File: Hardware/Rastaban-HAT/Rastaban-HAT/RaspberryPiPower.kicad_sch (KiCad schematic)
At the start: 19 parts, among them IC2 DMMT5401-7-F, Q3 DMG2305UX-7, U5 RT7272AGSP

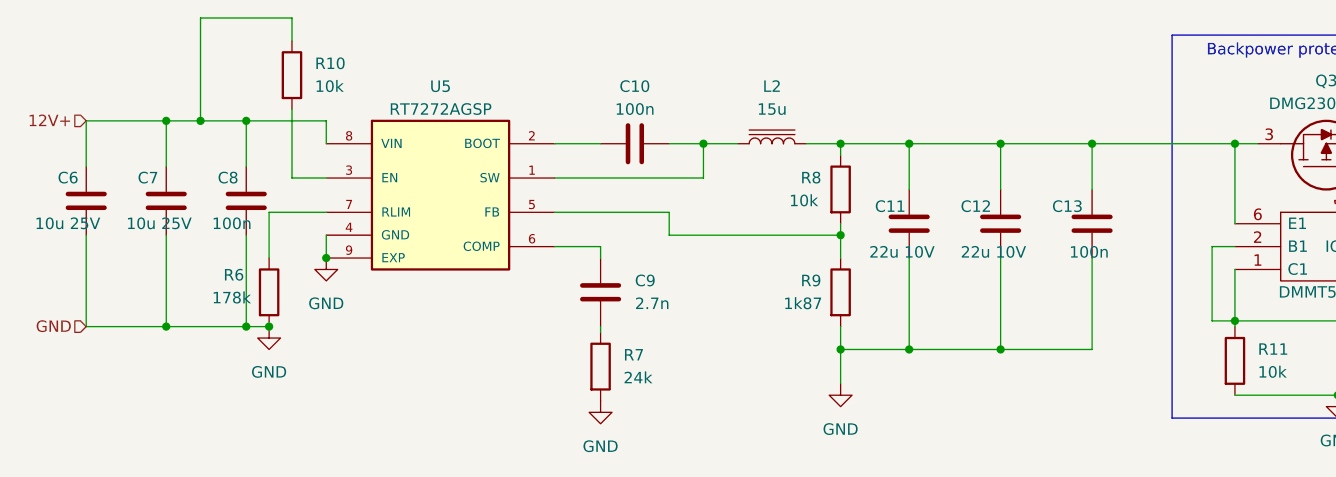
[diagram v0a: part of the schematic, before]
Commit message: added new libarries and jlcpcb part plugin
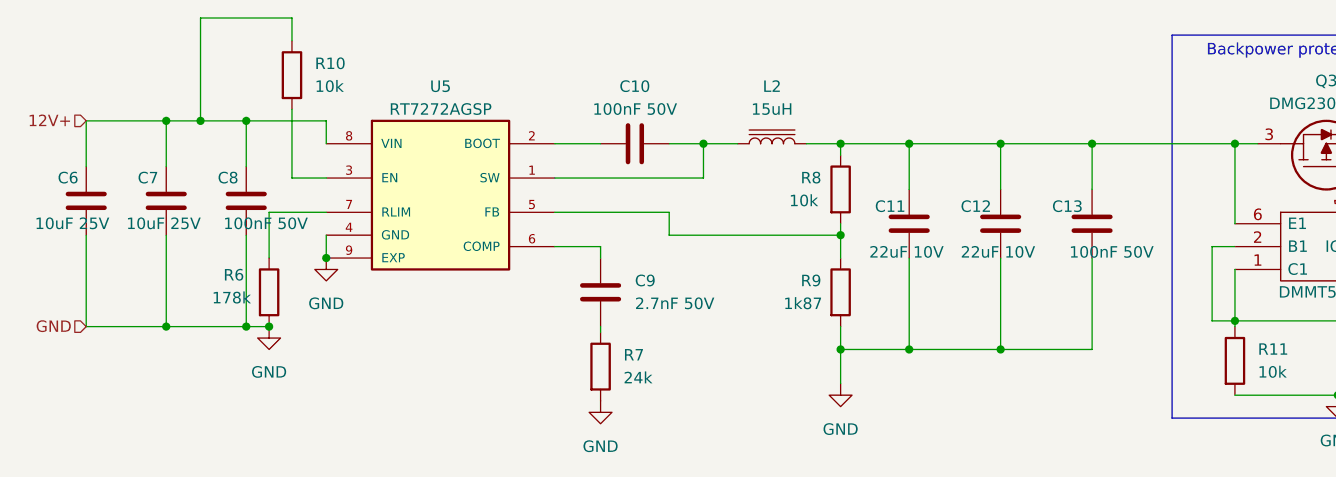
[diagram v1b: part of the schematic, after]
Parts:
- C10, C13, C8: value 100n -> 100nF 50V; footprint Capacitor_SMD:C_1206_3216Metric_Pad1.33x1.80mm_HandSolder -> Capacitor_SMD:C_0805_2012Metric_Pad1.18x1.45mm_HandSolder
- C11, C12: value 22u 10V -> 22uF 10V; footprint Capacitor_SMD:C_1206_3216Metric_Pad1.33x1.80mm_HandSolder -> Capacitor_SMD:C_0805_2012Metric_Pad1.18x1.45mm_HandSolder
- C6, C7: value 10u 25V -> 10uF 25V; footprint Capacitor_SMD:C_1206_3216Metric_Pad1.33x1.80mm_HandSolder -> Capacitor_SMD:C_0805_2012Metric_Pad1.18x1.45mm_HandSolder
- C9: value 2.7n -> 2.7nF 50V; footprint Capacitor_SMD:C_1206_3216Metric_Pad1.33x1.80mm_HandSolder -> Capacitor_SMD:C_0805_2012Metric_Pad1.18x1.45mm_HandSolder
- IC2: footprint SmacSYs:SOT95P285X140-6N -> SamacSys_Parts:SOT95P285X140-6N
- L2: value 15u -> 15uH
- Q3: footprint Snapeda:SOT91P240X110-3N_DMG2305UX-7 -> Package_TO_SOT_SMD:SOT-23
- R10, R11, R12, R6, R7, R8, R9: footprint Resistor_SMD:R_1206_3216Metric_Pad1.30x1.75mm_HandSolder -> Resistor_SMD:R_0805_2012Metric_Pad1.20x1.40mm_HandSolder
- U5: footprint Snapeda:SOIC127P599X175-9N -> (none)
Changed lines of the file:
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@@
       (effects (font (size 1.27 1.27)) (justify left))
     )
-    (property "Footprint" "Resistor_SMD:R_1206_3216Metric_Pad1.30x1.75mm_HandSolder" (id 2) (at 243.967 118.11 90)
+    (property "Footprint" "Resistor_SMD:R_0805_2012Metric_Pad1.20x1.40mm_HandSolder" (id 2) (at 243.967 118.11 90)
       (effects (font (size 1.27 1.27)) hide)
     )
@@
     (property "Reference" "Q3" (id 0) (at 233.045 86.995 90))
     (property "Value" "DMG2305UX-7" (id 1) (at 233.045 89.535 90))
-    (property "Footprint" "Snapeda:SOT91P240X110-3N_DMG2305UX-7" (id 2) (at 236.855 90.17 0)
+    (property "Footprint" "Package_TO_SOT_SMD:SOT-23" (id 2) (at 236.855 90.17 0)
       (effects (font (size 1.27 1.27)) (justify left) hide)
     )
@@
       (effects (font (size 1.27 1.27)) (justify left))
     )
-    (property "Footprint" "Resistor_SMD:R_1206_3216Metric_Pad1.30x1.75mm_HandSolder" (id 2) (at 116.332 86.36 90)
+    (property "Footprint" "Resistor_SMD:R_0805_2012Metric_Pad1.20x1.40mm_HandSolder" (id 2) (at 116.332 86.36 90)
       (effects (font (size 1.27 1.27)) hide)
     )
@@
       (effects (font (size 1.27 1.27)) (justify left))
     )
-    (property "Footprint" "Resistor_SMD:R_1206_3216Metric_Pad1.30x1.75mm_HandSolder" (id 2) (at 150.622 118.745 90)
+    (property "Footprint" "Resistor_SMD:R_0805_2012Metric_Pad1.20x1.40mm_HandSolder" (id 2) (at 150.622 118.745 90)
       (effects (font (size 1.27 1.27)) hide)
     )
@@
       (effects (font (size 1.27 1.27)) (justify left))
     )
-    (property "Footprint" "Resistor_SMD:R_1206_3216Metric_Pad1.30x1.75mm_HandSolder" (id 2) (at 113.792 110.49 90)
+    (property "Footprint" "Resistor_SMD:R_0805_2012Metric_Pad1.20x1.40mm_HandSolder" (id 2) (at 113.792 110.49 90)
       (effects (font (size 1.27 1.27)) hide)
     )
@@
       (effects (font (size 1.27 1.27)) (justify left))
     )
-    (property "Footprint" "Resistor_SMD:R_1206_3216Metric_Pad1.30x1.75mm_HandSolder" (id 2) (at 221.107 118.11 90)
+    (property "Footprint" "Resistor_SMD:R_0805_2012Metric_Pad1.20x1.40mm_HandSolder" (id 2) (at 221.107 118.11 90)
       (effects (font (size 1.27 1.27)) hide)
     )
@@
       (effects (font (size 1.27 1.27)) (justify right))
     )
-    (property "Value" "22u 10V" (id 1) (at 182.245 106.045 0)
-      (effects (font (size 1.27 1.27)) (justify right))
-    )
-    (property "Footprint" "Capacitor_SMD:C_1206_3216Metric_Pad1.33x1.80mm_HandSolder" (id 2) (at 185.7248 99.06 0)
+    (property "Value" "22uF 10V" (id 1) (at 182.245 106.045 0)
+      (effects (font (size 1.27 1.27)) (justify right))
+    )
+    (property "Footprint" "Capacitor_SMD:C_0805_2012Metric_Pad1.18x1.45mm_HandSolder" (id 2) (at 185.7248 99.06 0)
       (effects (font (size 1.27 1.27)) hide)
     )
@@
       (effects (font (size 1.27 1.27)) (justify left))
     )
-    (property "Value" "10u 25V" (id 1) (at 89.535 102.87 0)
-      (effects (font (size 1.27 1.27)) (justify left))
-    )
-    (property "Footprint" "Capacitor_SMD:C_1206_3216Metric_Pad1.33x1.80mm_HandSolder" (id 2) (at 96.2152 104.14 0)
+    (property "Value" "10uF 25V" (id 1) (at 89.535 102.87 0)
+      (effects (font (size 1.27 1.27)) (justify left))
+    )
+    (property "Footprint" "Capacitor_SMD:C_0805_2012Metric_Pad1.18x1.45mm_HandSolder" (id 2) (at 96.2152 104.14 0)
       (effects (font (size 1.27 1.27)) hide)
     )
@@
       (effects (font (size 1.27 1.27)) (justify right))
     )
-    (property "Value" "100n" (id 1) (at 204.47 106.045 0)
-      (effects (font (size 1.27 1.27)) (justify right))
-    )
-    (property "Footprint" "Capacitor_SMD:C_1206_3216Metric_Pad1.33x1.80mm_HandSolder" (id 2) (at 206.0448 99.06 0)
+    (property "Value" "100nF 50V" (id 1) (at 204.47 106.045 0)
+      (effects (font (size 1.27 1.27)) (justify right))
+    )
+    (property "Footprint" "Capacitor_SMD:C_0805_2012Metric_Pad1.18x1.45mm_HandSolder" (id 2) (at 206.0448 99.06 0)
       (effects (font (size 1.27 1.27)) hide)
     )
@@
       (effects (font (size 1.27 1.27)) (justify left))
     )
-    (property "Value" "10u 25V" (id 1) (at 99.695 102.87 0)
-      (effects (font (size 1.27 1.27)) (justify left))
-    )
-    (property "Footprint" "Capacitor_SMD:C_1206_3216Metric_Pad1.33x1.80mm_HandSolder" (id 2) (at 105.1052 104.14 0)
+    (property "Value" "10uF 25V" (id 1) (at 99.695 102.87 0)
+      (effects (font (size 1.27 1.27)) (justify left))
+    )
+    (property "Footprint" "Capacitor_SMD:C_0805_2012Metric_Pad1.18x1.45mm_HandSolder" (id 2) (at 105.1052 104.14 0)
       (effects (font (size 1.27 1.27)) hide)
     )
@@
     (property "Reference" "U5" (id 0) (at 134.62 87.63 0))
     (property "Value" "RT7272AGSP" (id 1) (at 134.62 90.17 0))
-    (property "Footprint" "Snapeda:SOIC127P599X175-9N" (id 2) (at 127 110.49 0)
+    (property "Footprint" "" (id 2) (at 127 110.49 0)
       (effects (font (size 1.27 1.27)) (justify left bottom) hide)
     )
@@
       (effects (font (size 1.27 1.27)) (justify right))
     )
-    (property "Value" "2.7n" (id 1) (at 156.21 111.7599 0)
-      (effects (font (size 1.27 1.27)) (justify right))
-    )
-    (property "Footprint" "Capacitor_SMD:C_1206_3216Metric_Pad1.33x1.80mm_HandSolder" (id 2) (at 151.4348 106.68 0)
+    (property "Value" "2.7nF 50V" (id 1) (at 156.21 111.7599 0)
+      (effects (font (size 1.27 1.27)) (justify right))
+    )
+    (property "Footprint" "Capacitor_SMD:C_0805_2012Metric_Pad1.18x1.45mm_HandSolder" (id 2) (at 151.4348 106.68 0)
       (effects (font (size 1.27 1.27)) hide)
     )
@@
     (property "Reference" "IC2" (id 0) (at 234.315 105.41 0))
     (property "Value" "DMMT5401-7-F" (id 1) (at 234.315 110.49 0))
-    (property "Footprint" "SmacSYs:SOT95P285X140-6N" (id 2) (at 241.935 100.33 0)
+    (property "Footprint" "SamacSys_Parts:SOT95P285X140-6N" (id 2) (at 241.935 100.33 0)
       (effects (font (size 1.27 1.27)) (justify left) hide)
     )
@@
       (effects (font (size 1.27 1.27)) (justify right))
     )
-    (property "Value" "22u 10V" (id 1) (at 192.405 106.045 0)
-      (effects (font (size 1.27 1.27)) (justify right))
-    )
-    (property "Footprint" "Capacitor_SMD:C_1206_3216Metric_Pad1.33x1.80mm_HandSolder" (id 2) (at 195.8848 99.06 0)
+    (property "Value" "22uF 10V" (id 1) (at 192.405 106.045 0)
+      (effects (font (size 1.27 1.27)) (justify right))
+    )
+    (property "Footprint" "Capacitor_SMD:C_0805_2012Metric_Pad1.18x1.45mm_HandSolder" (id 2) (at 195.8848 99.06 0)
       (effects (font (size 1.27 1.27)) hide)
     )
@@
       (effects (font (size 1.27 1.27)) (justify left))
     )
-    (property "Footprint" "Resistor_SMD:R_1206_3216Metric_Pad1.30x1.75mm_HandSolder" (id 2) (at 177.292 99.06 90)
+    (property "Footprint" "Resistor_SMD:R_0805_2012Metric_Pad1.20x1.40mm_HandSolder" (id 2) (at 177.292 99.06 90)
       (effects (font (size 1.27 1.27)) hide)
     )
@@
       (effects (font (size 1.27 1.27)) (justify left))
     )
-    (property "Footprint" "Resistor_SMD:R_1206_3216Metric_Pad1.30x1.75mm_HandSolder" (id 2) (at 177.292 110.49 90)
+    (property "Footprint" "Resistor_SMD:R_0805_2012Metric_Pad1.20x1.40mm_HandSolder" (id 2) (at 177.292 110.49 90)
       (effects (font (size 1.27 1.27)) hide)
     )
@@
     (in_bom yes) (on_board yes)
     (property "Reference" "C10" (id 0) (at 156.21 87.63 90))
-    (property "Value" "100n" (id 1) (at 156.21 90.17 90))
-    (property "Footprint" "Capacitor_SMD:C_1206_3216Metric_Pad1.33x1.80mm_HandSolder" (id 2) (at 160.02 93.0148 0)
+    (property "Value" "100nF 50V" (id 1) (at 156.21 90.17 90))
+    (property "Footprint" "Capacitor_SMD:C_0805_2012Metric_Pad1.18x1.45mm_HandSolder" (id 2) (at 160.02 93.0148 0)
       (effects (font (size 1.27 1.27)) hide)
     )
@@
       (effects (font (size 1.27 1.27)) (justify left))
     )
-    (property "Value" "100n" (id 1) (at 109.22 102.87 0)
-      (effects (font (size 1.27 1.27)) (justify left))
-    )
-    (property "Footprint" "Capacitor_SMD:C_1206_3216Metric_Pad1.33x1.80mm_HandSolder" (id 2) (at 113.9952 104.14 0)
+    (property "Value" "100nF 50V" (id 1) (at 110.49 102.87 0)
+      (effects (font (size 1.27 1.27)) (justify left))
+    )
+    (property "Footprint" "Capacitor_SMD:C_0805_2012Metric_Pad1.18x1.45mm_HandSolder" (id 2) (at 113.9952 104.14 0)
       (effects (font (size 1.27 1.27)) hide)
     )
@@
     (in_bom yes) (on_board yes) (fields_autoplaced)
     (property "Reference" "L2" (id 0) (at 171.45 87.63 90))
-    (property "Value" "15u" (id 1) (at 171.45 90.17 90))
+    (property "Value" "15uH" (id 1) (at 171.45 90.17 90))
     (property "Footprint" "Inductor_SMD:L_1206_3216Metric_Pad1.22x1.90mm_HandSolder" (id 2) (at 171.45 93.98 0)
       (effects (font (size 1.27 1.27)) hide)

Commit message: updated footprints
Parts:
- U5: footprint (none) -> SnapEDA Library:SOIC127P599X175-9N
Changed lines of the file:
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@@
     (property "Reference" "U5" (id 0) (at 134.62 87.63 0))
     (property "Value" "RT7272AGSP" (id 1) (at 134.62 90.17 0))
-    (property "Footprint" "" (id 2) (at 127 110.49 0)
+    (property "Footprint" "SnapEDA Library:SOIC127P599X175-9N" (id 2) (at 127 110.49 0)
       (effects (font (size 1.27 1.27)) (justify left bottom) hide)
     )

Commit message: changed capacitor footprints
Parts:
- C11, C12: footprint Capacitor_SMD:C_0805_2012Metric_Pad1.18x1.45mm_HandSolder -> Capacitor_SMD:CP_Elec_6.3x7.7
- C13, C8: footprint Capacitor_SMD:C_0805_2012Metric_Pad1.18x1.45mm_HandSolder -> Capacitor_SMD:CP_Elec_4x5.4
- C6, C7: footprint Capacitor_SMD:C_0805_2012Metric_Pad1.18x1.45mm_HandSolder -> Capacitor_SMD:CP_Elec_3x5.4
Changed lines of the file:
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@@
       (effects (font (size 1.27 1.27)) (justify right))
     )
-    (property "Footprint" "Capacitor_SMD:C_0805_2012Metric_Pad1.18x1.45mm_HandSolder" (id 2) (at 185.7248 99.06 0)
+    (property "Footprint" "Capacitor_SMD:CP_Elec_6.3x7.7" (id 2) (at 185.7248 99.06 0)
       (effects (font (size 1.27 1.27)) hide)
     )
@@
       (effects (font (size 1.27 1.27)) (justify left))
     )
-    (property "Footprint" "Capacitor_SMD:C_0805_2012Metric_Pad1.18x1.45mm_HandSolder" (id 2) (at 96.2152 104.14 0)
+    (property "Footprint" "Capacitor_SMD:CP_Elec_3x5.4" (id 2) (at 96.2152 104.14 0)
       (effects (font (size 1.27 1.27)) hide)
     )
@@
       (effects (font (size 1.27 1.27)) (justify right))
     )
-    (property "Footprint" "Capacitor_SMD:C_0805_2012Metric_Pad1.18x1.45mm_HandSolder" (id 2) (at 206.0448 99.06 0)
+    (property "Footprint" "Capacitor_SMD:CP_Elec_4x5.4" (id 2) (at 206.0448 99.06 0)
       (effects (font (size 1.27 1.27)) hide)
     )
@@
       (effects (font (size 1.27 1.27)) (justify left))
     )
-    (property "Footprint" "Capacitor_SMD:C_0805_2012Metric_Pad1.18x1.45mm_HandSolder" (id 2) (at 105.1052 104.14 0)
+    (property "Footprint" "Capacitor_SMD:CP_Elec_3x5.4" (id 2) (at 105.1052 104.14 0)
       (effects (font (size 1.27 1.27)) hide)
     )
@@
       (effects (font (size 1.27 1.27)) (justify right))
     )
-    (property "Footprint" "Capacitor_SMD:C_0805_2012Metric_Pad1.18x1.45mm_HandSolder" (id 2) (at 195.8848 99.06 0)
+    (property "Footprint" "Capacitor_SMD:CP_Elec_6.3x7.7" (id 2) (at 195.8848 99.06 0)
       (effects (font (size 1.27 1.27)) hide)
     )
@@
       (effects (font (size 1.27 1.27)) (justify left))
     )
-    (property "Footprint" "Capacitor_SMD:C_0805_2012Metric_Pad1.18x1.45mm_HandSolder" (id 2) (at 113.9952 104.14 0)
-      (effects (font (size 1.27 1.27)) hide)
-    )
+    (property "Footprint" "Capacitor_SMD:CP_Elec_4x5.4" (id 2) (at 113.9952 104.14 0)
+      (effects (font (size 1.27 1.27)) hide)
+    )
